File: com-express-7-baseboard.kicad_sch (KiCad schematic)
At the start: 0 parts

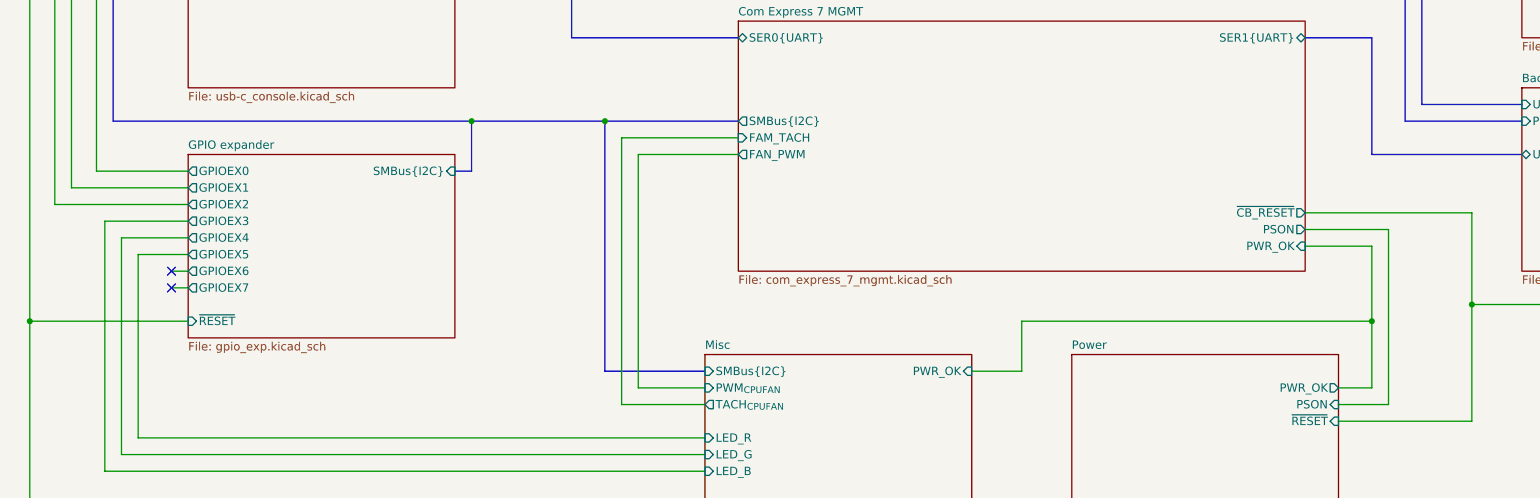
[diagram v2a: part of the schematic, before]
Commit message: [#58137] Add power monitors; clean up I2C bus
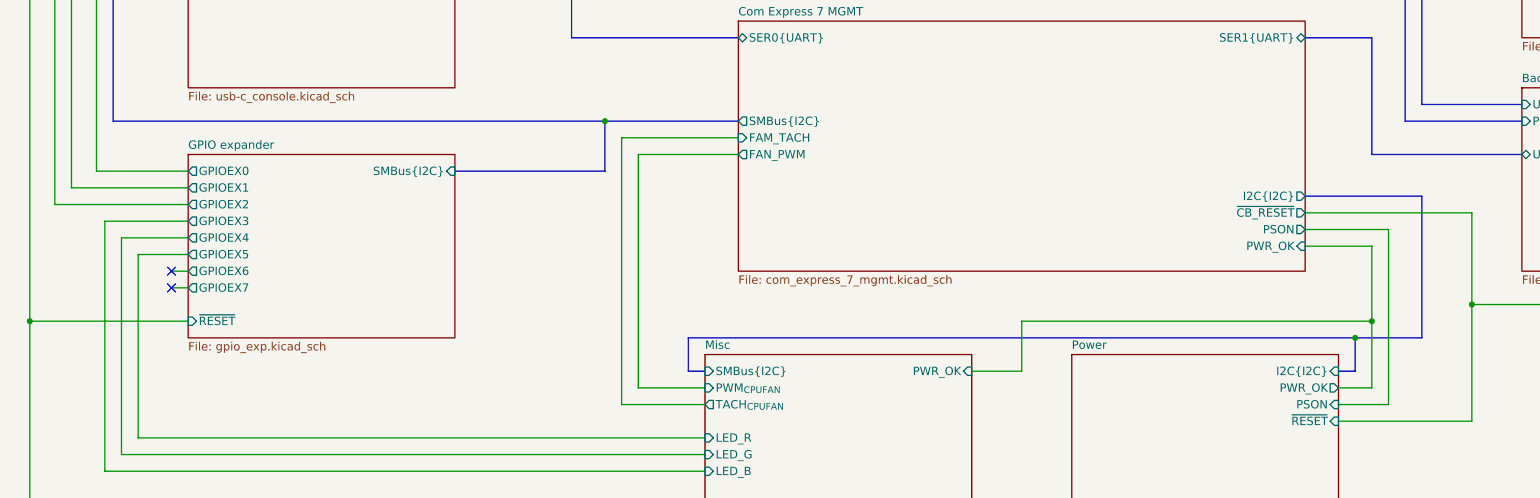
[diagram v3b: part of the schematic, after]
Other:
- sheet Com Express 7 MGMT ports: added I2C{I2C}; removed none
- sheet Power ports: added I2C{I2C}; removed none
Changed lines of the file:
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@@
   (junction (at 274.32 236.22) (diameter 0) (color 0 0 0 0)
   )
-  (junction (at 121.92 208.28) (diameter 0) (color 0 0 0 0)
-  )
   (junction (at 327.66 104.14) (diameter 0) (color 0 0 0 0)
   )
@@
   (junction (at 325.12 101.6) (diameter 0) (color 0 0 0 0)
   )
+  (junction (at 54.61 144.78) (diameter 0) (color 0 0 0 0)
+  )
   (junction (at 142.24 208.28) (diameter 0) (color 0 0 0 0)
   )
-  (junction (at 54.61 144.78) (diameter 0) (color 0 0 0 0)
-  )
   (junction (at 64.77 171.45) (diameter 0) (color 0 0 0 0)
   )
@@
   )
   (junction (at 327.66 68.58) (diameter 0) (color 0 0 0 0)
+  )
+  (junction (at 256.54 241.3) (diameter 0) (color 0 0 0 0)
   )
   (no_connect (at 76.2 231.14))
@@
     (stroke (width 0) (type default) (color 0 0 255 1))
   )
+  (bus (pts (xy 256.54 241.3) (xy 266.7 241.3))
+    (stroke (width 0) (type default))
+  )
   (bus (pts (xy 119.38 76.2) (xy 162.56 76.2))
     (stroke (width 0) (type default) (color 0 255 255 1))
@@
     (stroke (width 0) (type default))
   )
+  (bus (pts (xy 142.24 208.28) (xy 142.24 215.9))
+    (stroke (width 0) (type default))
+  )
   (bus (pts (xy 332.74 71.12) (xy 332.74 30.48))
     (stroke (width 0) (type default))
@@
   )
   (bus (pts (xy 337.82 142.24) (xy 337.82 25.4))
+    (stroke (width 0) (type default))
+  )
+  (bus (pts (xy 154.94 241.3) (xy 154.94 246.38))
     (stroke (width 0) (type default))
   )
@@
     (stroke (width 0) (type default))
   )
+  (bus (pts (xy 254 246.38) (xy 256.54 246.38))
+    (stroke (width 0) (type default))
+  )
   (wire (pts (xy 78.74 218.44) (xy 60.96 218.44))
     (stroke (width 0) (type default))
@@
     (stroke (width 0) (type default))
   )
+  (bus (pts (xy 266.7 219.71) (xy 266.7 241.3))
+    (stroke (width 0) (type default))
+  )
   (bus (pts (xy 119.38 81.28) (xy 162.56 81.28))
     (stroke (width 0) (type default) (color 0 0 255 1))
@@
     (stroke (width 0) (type default))
   )
-  (bus (pts (xy 157.48 246.38) (xy 142.24 246.38))
+  (bus (pts (xy 157.48 246.38) (xy 154.94 246.38))
     (stroke (width 0) (type default))
   )
@@
     (stroke (width 0) (type default))
   )
-  (bus (pts (xy 119.38 215.9) (xy 121.92 215.9))
-    (stroke (width 0) (type default))
-  )
-  (bus (pts (xy 121.92 208.28) (xy 121.92 215.9))
+  (bus (pts (xy 119.38 215.9) (xy 142.24 215.9))
     (stroke (width 0) (type default))
   )
@@
     (stroke (width 0) (type default))
   )
+  (bus (pts (xy 154.94 241.3) (xy 256.54 241.3))
+    (stroke (width 0) (type default))
+  )
   (bus (pts (xy 76.2 129.54) (xy 76.2 135.89))
     (stroke (width 0) (type default))
@@
     (stroke (width 0) (type default))
   )
+  (bus (pts (xy 142.24 208.28) (xy 162.56 208.28))
+    (stroke (width 0) (type default))
+  )
   (wire (pts (xy 157.48 256.54) (xy 71.12 256.54))
     (stroke (width 0) (type default))
   )
-  (bus (pts (xy 121.92 208.28) (xy 142.24 208.28))
-    (stroke (width 0) (type default))
-  )
   (wire (pts (xy 327.66 139.7) (xy 327.66 104.14))
     (stroke (width 0) (type default))
   )
   (wire (pts (xy 261.62 224.79) (xy 248.92 224.79))
-    (stroke (width 0) (type default))
-  )
-  (bus (pts (xy 142.24 208.28) (xy 162.56 208.28))
     (stroke (width 0) (type default))
   )
@@
     (stroke (width 0) (type default))
   )
-  (bus (pts (xy 67.31 208.28) (xy 121.92 208.28))
+  (bus (pts (xy 248.92 219.71) (xy 266.7 219.71))
+    (stroke (width 0) (type default))
+  )
+  (bus (pts (xy 67.31 208.28) (xy 142.24 208.28))
     (stroke (width 0) (type default))
   )
@@
     (stroke (width 0) (type default))
   )
-  (bus (pts (xy 142.24 246.38) (xy 142.24 208.28))
-    (stroke (width 0) (type default))
-  )
   (bus (pts (xy 78.74 129.54) (xy 76.2 129.54))
     (stroke (width 0) (type default))
@@
   )
   (wire (pts (xy 78.74 238.76) (xy 54.61 238.76))
+    (stroke (width 0) (type default))
+  )
+  (bus (pts (xy 256.54 246.38) (xy 256.54 241.3))
     (stroke (width 0) (type default))
   )
@@
       (effects (font (size 1.27 1.27)) (justify right))
     )
+    (pin "I2C{I2C}" input (at 254 246.38 0)
+      (effects (font (size 1.27 1.27)) (justify right))
+    )
     (instances
       (project "com-express-7-baseboard"
@@
       (effects (font (size 1.27 1.27)) (justify right))
     )
+    (pin "I2C{I2C}" output (at 248.92 219.71 0)
+      (effects (font (size 1.27 1.27)) (justify right))
+    )

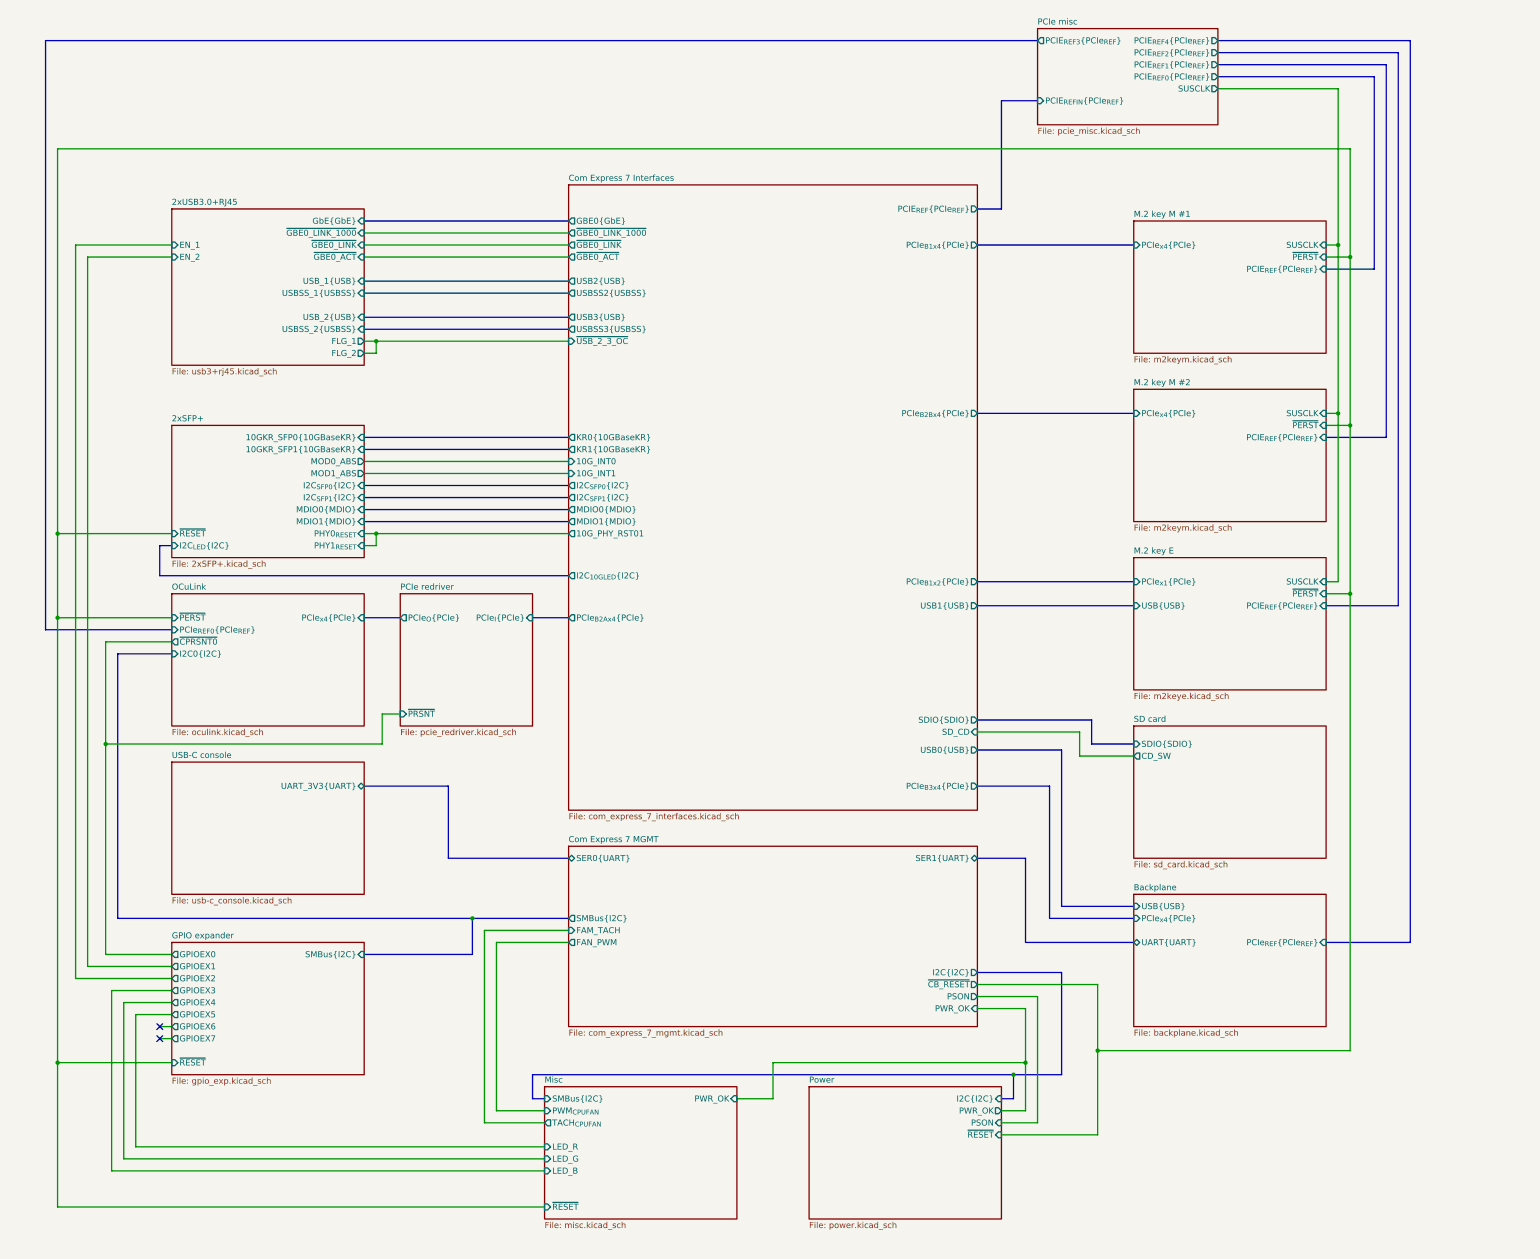
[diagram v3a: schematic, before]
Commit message: [#58904] Change pinout of backplane connector. Connect CLKREQ from PCIe devices
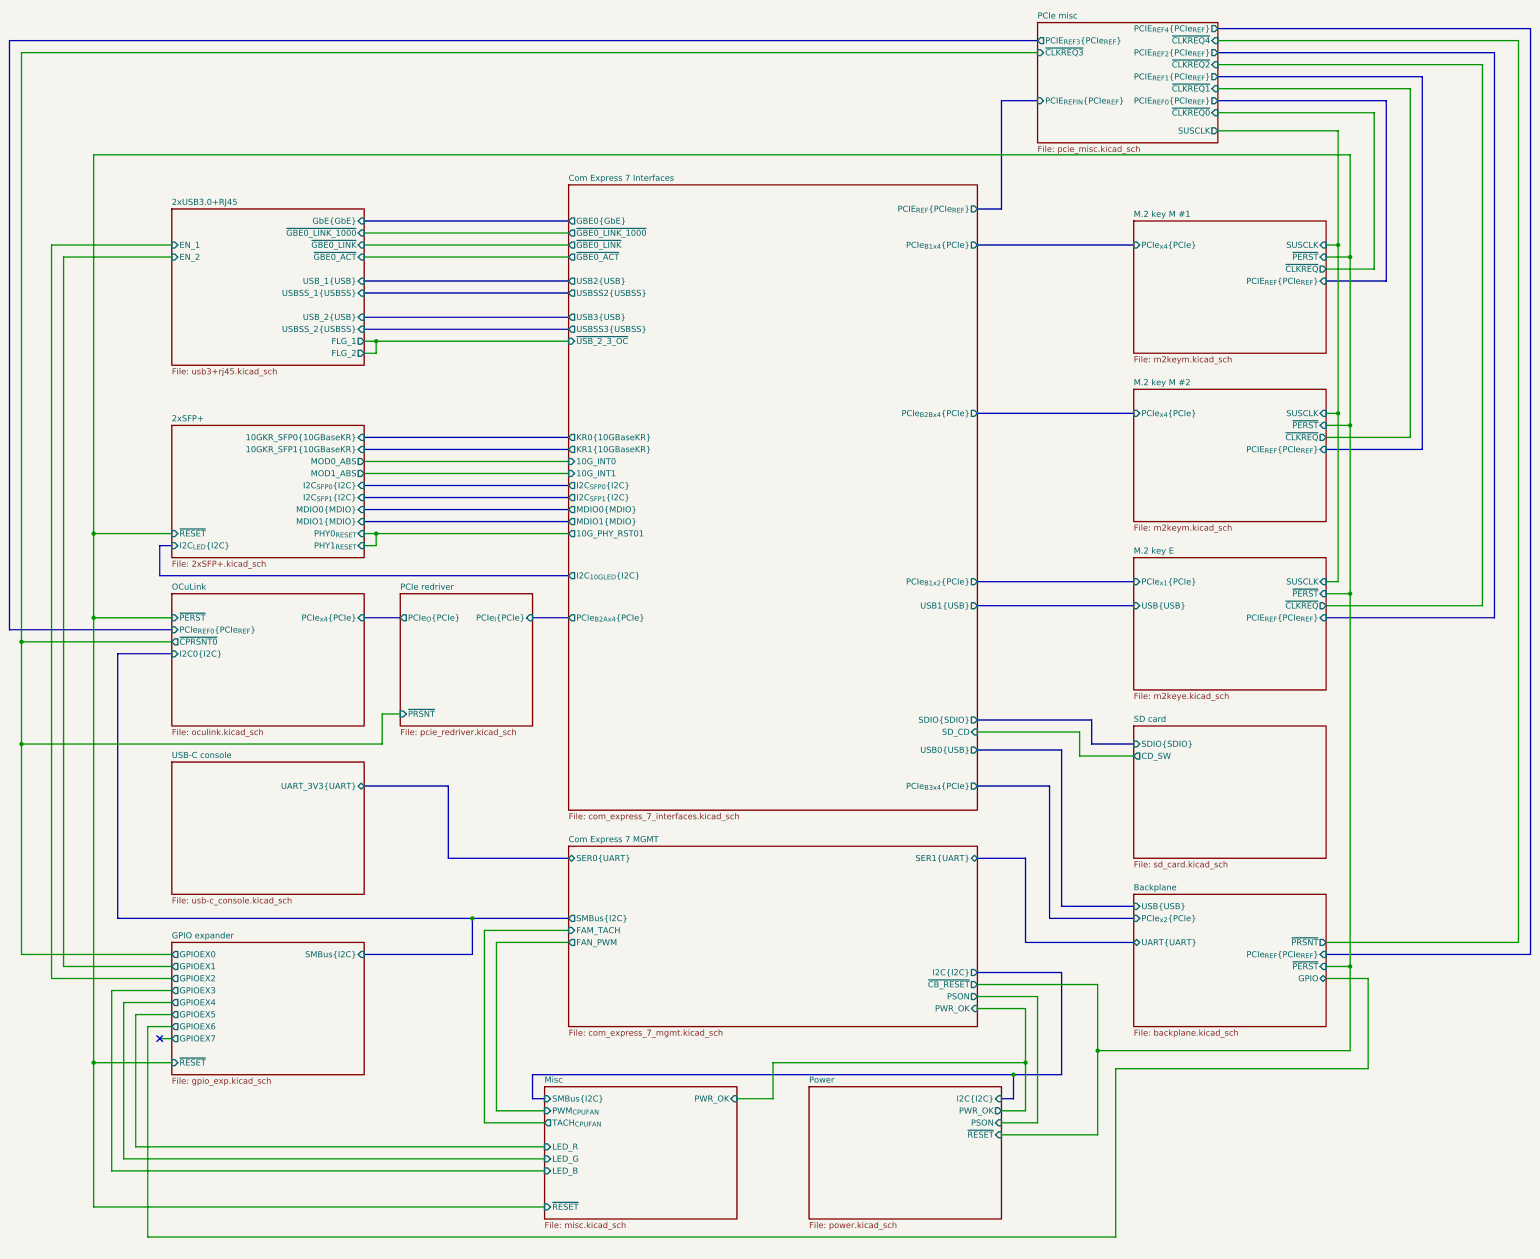
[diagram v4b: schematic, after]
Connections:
- no-connect marks 2 -> 1
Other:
- sheet Backplane ports: added GPIO, PCIe_{x2}{PCIe}, ~{PERST}, ~{PRSNT}; removed PCIe_{x4}{PCIe}
- sheet M.2 key E ports: added ~{CLKREQ}; removed none
- sheet M.2 key M #1 ports: added ~{CLKREQ}; removed none
- sheet M.2 key M #2 ports: added ~{CLKREQ}; removed none
- sheet PCIe misc ports: added ~{CLKREQ0}, ~{CLKREQ1}, ~{CLKREQ2}, ~{CLKREQ3}, ~{CLKREQ4}; removed none
